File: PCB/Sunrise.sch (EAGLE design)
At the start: 66 parts, among them IC1 STNS01, IC2 MT2492, J2 B2B-PH-K-S, J3 POWER_JACK, M1 E73-2G4M04S, Q1 IRLHM630, Q2 IRLHM630, Q3 IRLHM630

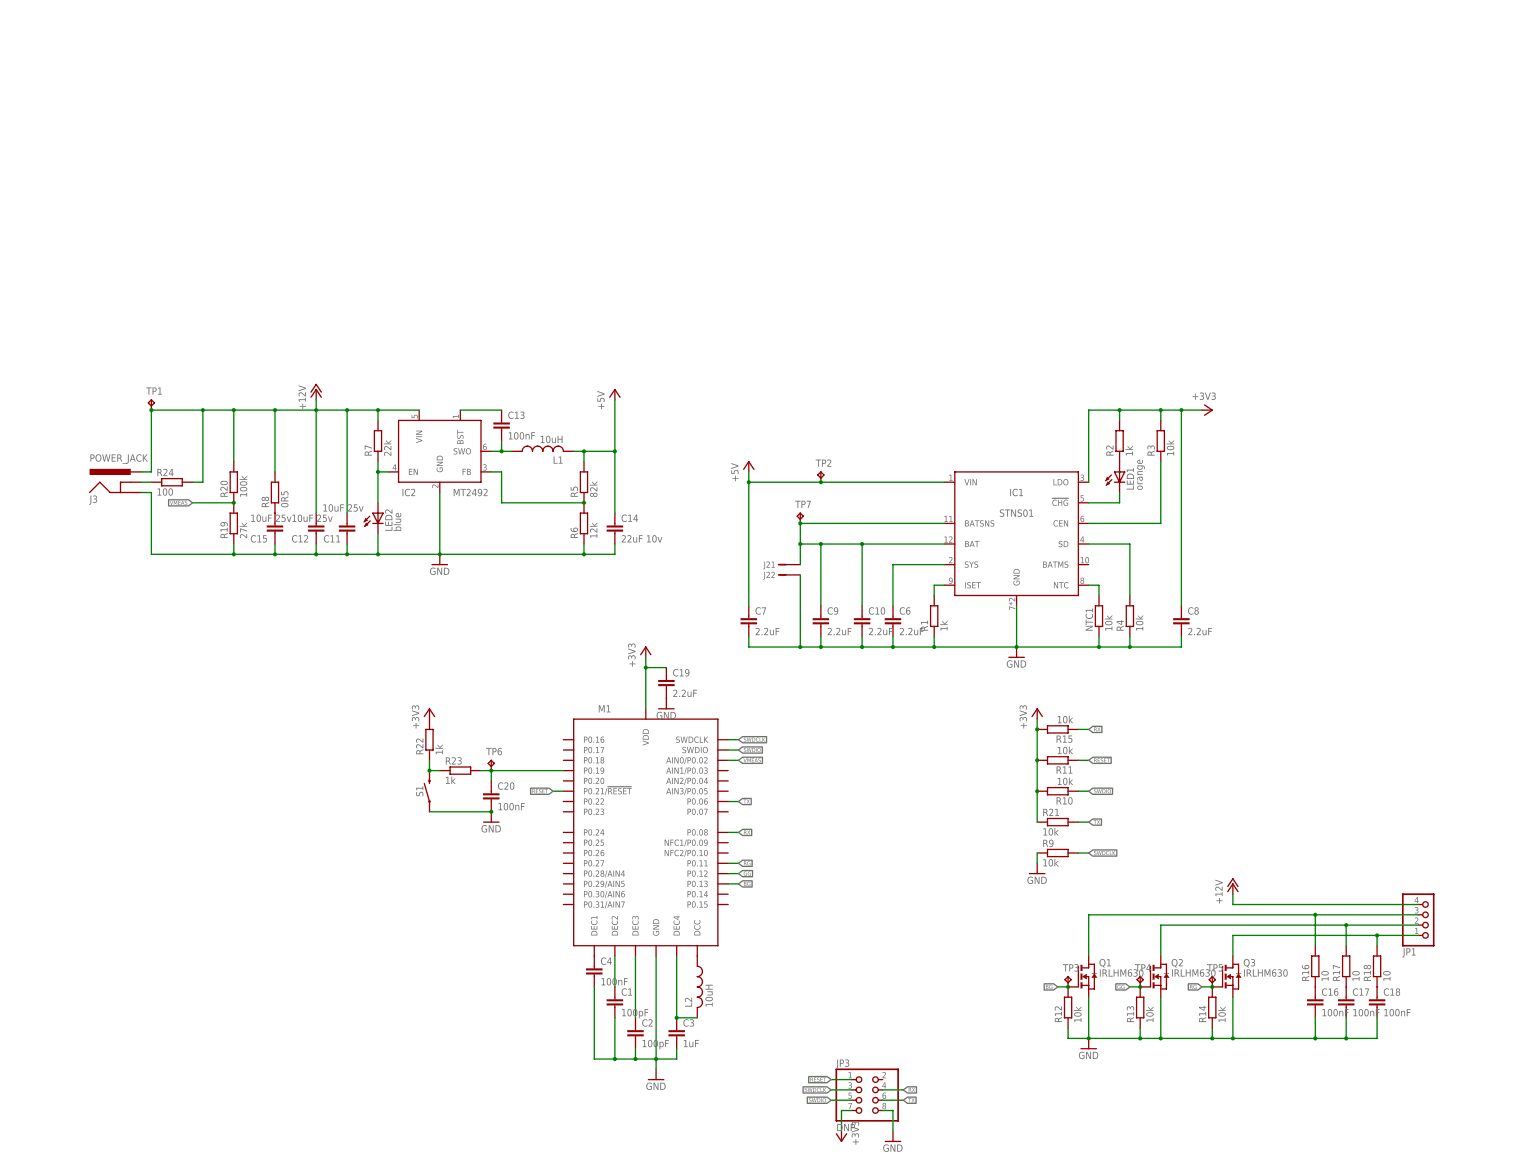
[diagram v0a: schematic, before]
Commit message: PCB: Clean schematic, move values on board around a bit, no actual connectivity or component changes
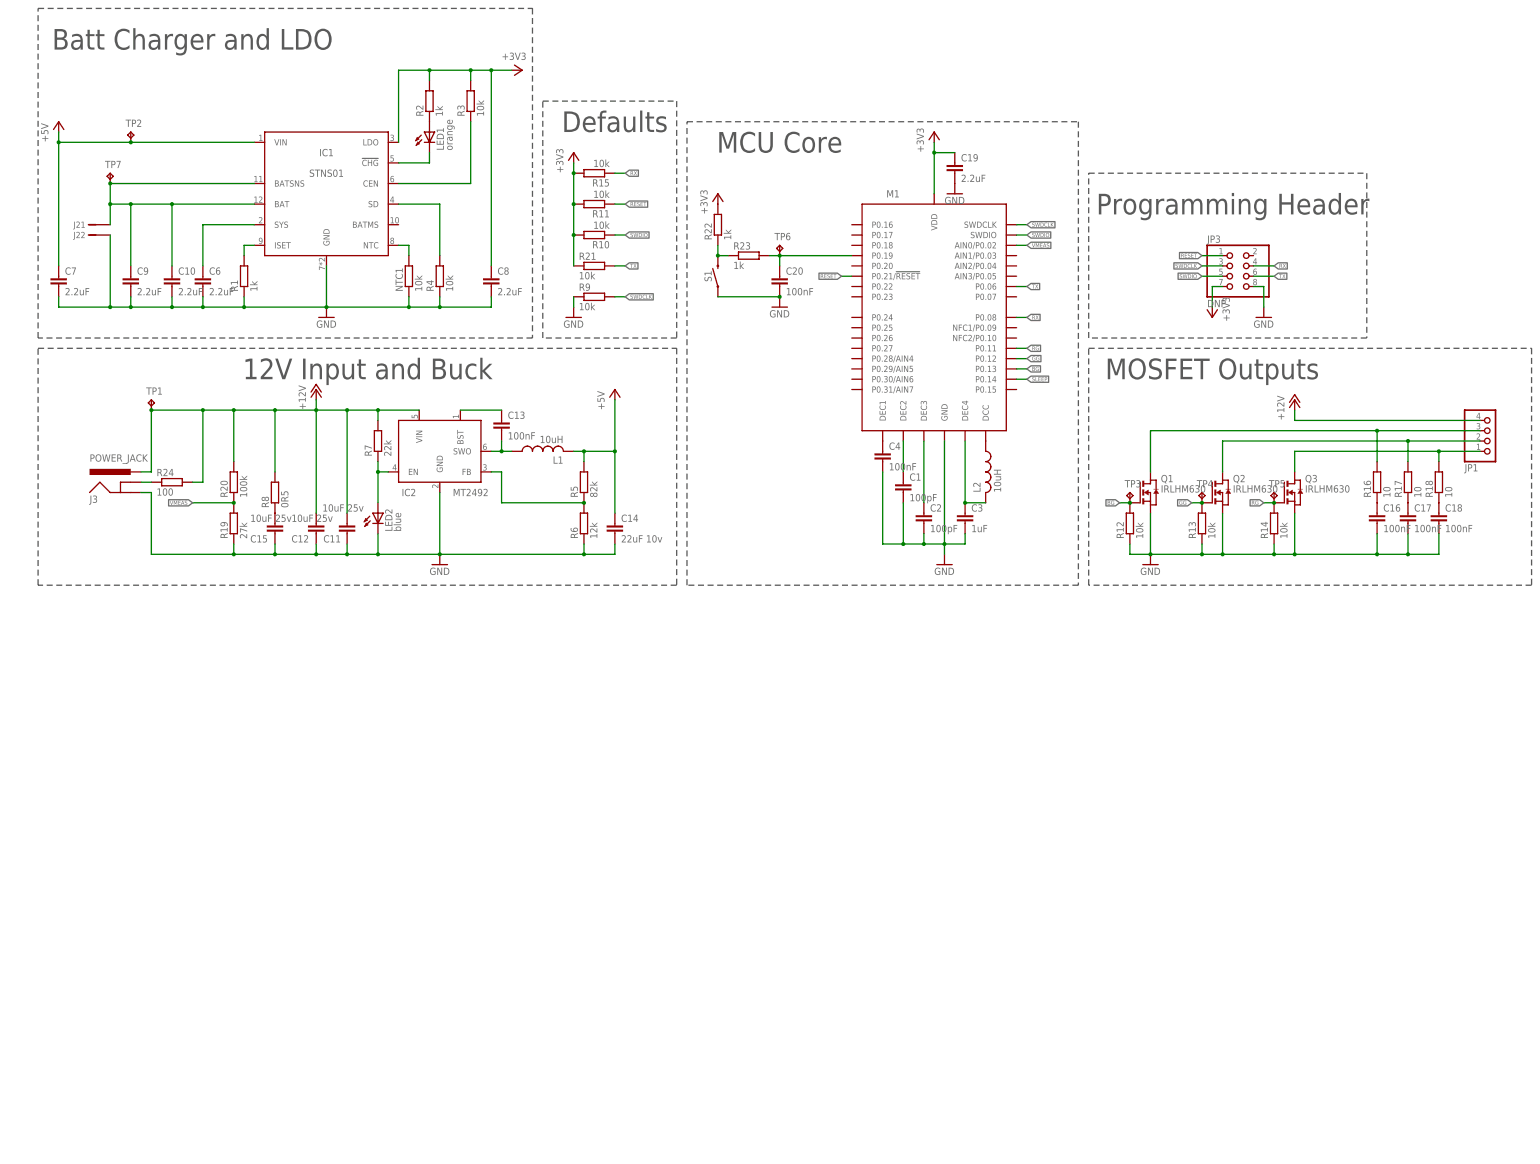
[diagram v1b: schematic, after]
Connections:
- new net SLEEP: M1.P0.14
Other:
- note added: "12V Input and Buck"
- note added: "Batt Charger and LDO"
- note added: "Defaults"
- note added: "MCU Core"
- note added: "MOSFET Outputs"
- note added: "Programming Header"
- moved on the sheet: C1, C10, C16, C17, C18, C19, C2, C20, C3, C4, C6, C7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

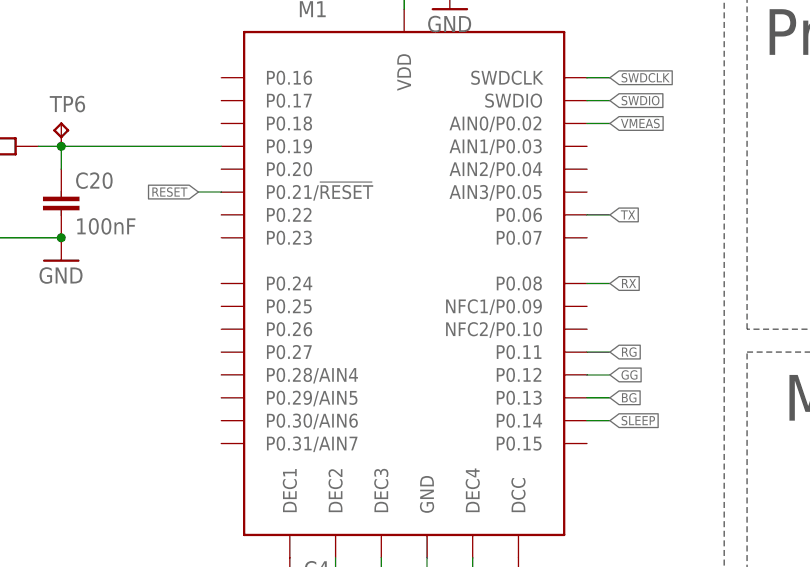
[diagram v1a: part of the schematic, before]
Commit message: PCB: Minor update to NRF52 module; specify a package variant and expand its description
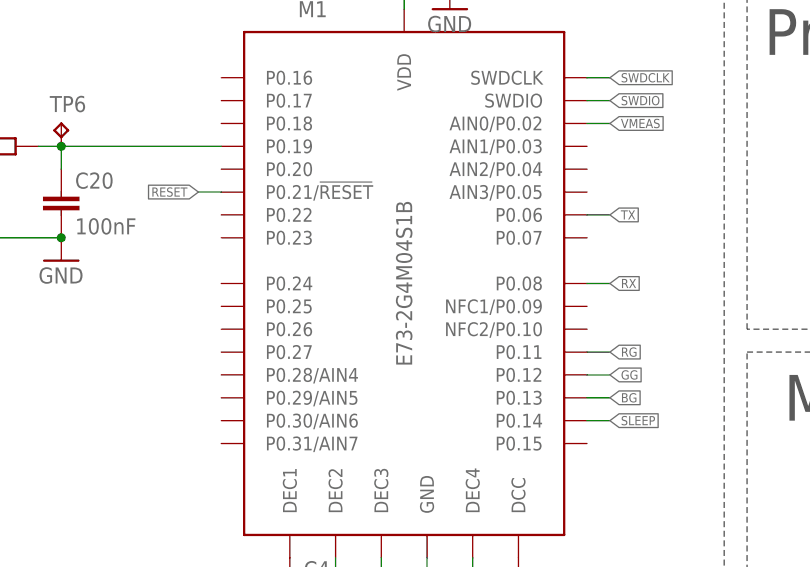
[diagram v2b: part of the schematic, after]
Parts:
- M1: value E73-2G4M04S -> E73-2G4M04S1B; device E73-2G4M04S:E73-2G4M04S -> E73-2G4M04S:E73-2G4M04S1B
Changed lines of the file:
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@@
 </classes>
 <parts>
-<part name="M1" library="E73-2G4M04S" deviceset="E73-2G4M04S" device=""/>
+<part name="M1" library="E73-2G4M04S" deviceset="E73-2G4M04S" device="1B" value="E73-2G4M04S1B"/>
 <part name="GND1" library="supply1" deviceset="GND" device=""/>
 <part name="C1" library="rcl" deviceset="C-EU" device="C0402K" value="100pF"/>

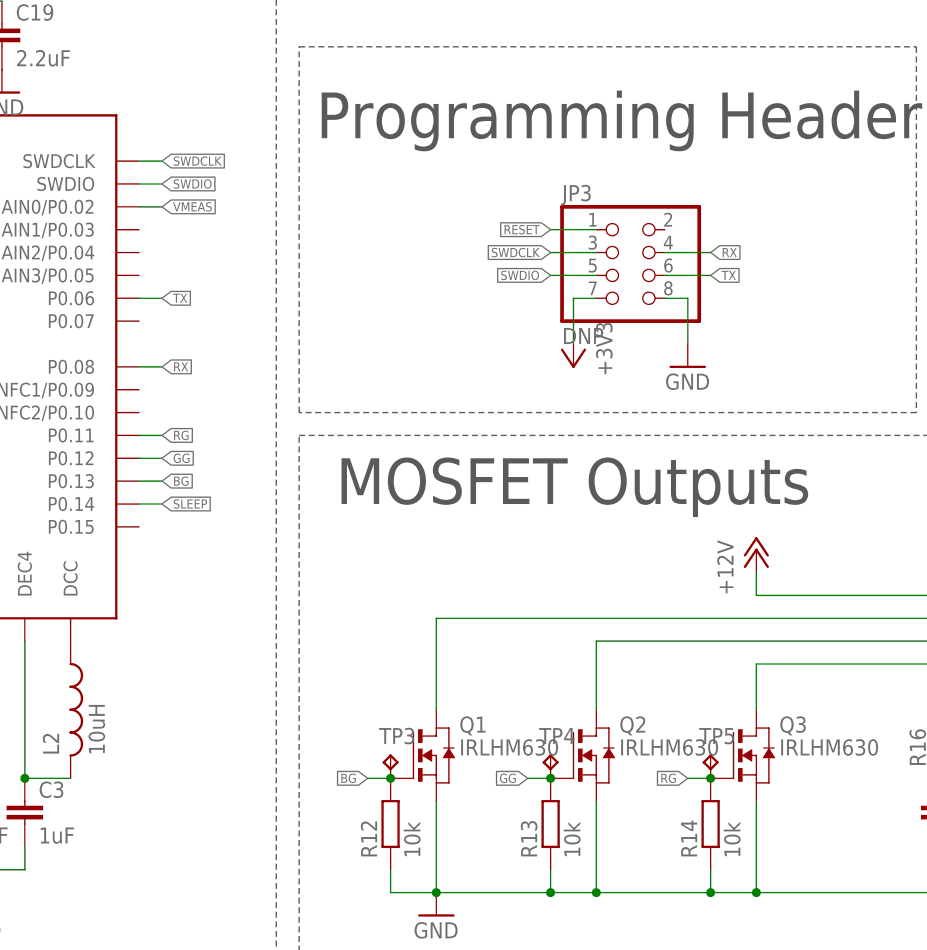
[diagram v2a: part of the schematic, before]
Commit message: Relabel red/green/blue channels to match common RGB strips
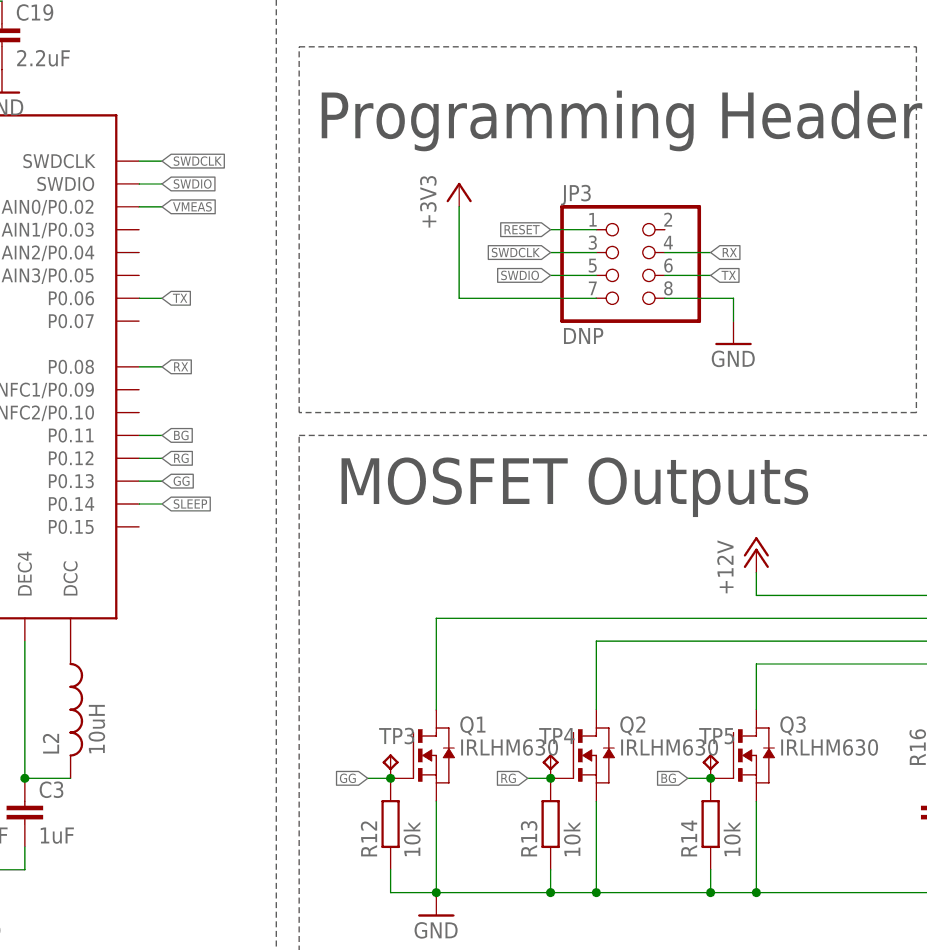
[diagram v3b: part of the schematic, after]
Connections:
- net BG: now also M1.P0.11, Q3.G, R14.2, TP5.TP; no longer M1.P0.13, Q1.G, R12.2, TP3.TP
- net GG: now also M1.P0.13, Q1.G, R12.2, TP3.TP; no longer M1.P0.12, Q2.G, R13.2, TP4.TP
- net RG: now also M1.P0.12, Q2.G, R13.2, TP4.TP; no longer M1.P0.11, Q3.G, R14.2, TP5.TP
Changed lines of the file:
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@@
 <attribute name="NAME" x="64.516" y="185.42" size="1.778" layer="95" font="vector" rot="R90" align="bottom-center"/>
 </instance>
-<instance part="GND9" gate="1" x="200.66" y="175.26"/>
-<instance part="+3V6" gate="G$1" x="187.96" y="175.26" rot="R180"/>
+<instance part="GND9" gate="1" x="205.74" y="177.8"/>
+<instance part="+3V6" gate="G$1" x="175.26" y="195.58"/>
 <instance part="R24" gate="G$1" x="-68.58" y="134.62"/>
 <instance part="L2" gate="G$1" x="132.08" y="137.16"/>
@@
 </segment>
 <segment>
-<wire x1="198.12" y1="182.88" x2="200.66" y2="182.88" width="0.1524" layer="91"/>
+<wire x1="198.12" y1="182.88" x2="205.74" y2="182.88" width="0.1524" layer="91"/>
 <pinref part="GND9" gate="1" pin="GND"/>
-<wire x1="200.66" y1="182.88" x2="200.66" y2="177.8" width="0.1524" layer="91"/>
+<wire x1="205.74" y1="182.88" x2="205.74" y2="180.34" width="0.1524" layer="91"/>
 <pinref part="JP3" gate="A" pin="8"/>
 </segment>
@@
 </segment>
 <segment>
-<wire x1="190.5" y1="182.88" x2="187.96" y2="182.88" width="0.1524" layer="91"/>
+<wire x1="190.5" y1="182.88" x2="175.26" y2="182.88" width="0.1524" layer="91"/>
 <pinref part="+3V6" gate="G$1" pin="+3V3"/>
-<wire x1="187.96" y1="182.88" x2="187.96" y2="177.8" width="0.1524" layer="91"/>
+<wire x1="175.26" y1="182.88" x2="175.26" y2="193.04" width="0.1524" layer="91"/>
 <pinref part="JP3" gate="A" pin="7"/>
 </segment>
@@
 </segment>
 </net>
-<net name="RG" class="0">
+<net name="BG" class="0">
 <segment>
 <pinref part="M1" gate="G$1" pin="P0.11"/>
@@
 </segment>
 </net>
-<net name="GG" class="0">
+<net name="RG" class="0">
 <segment>
 <pinref part="M1" gate="G$1" pin="P0.12"/>
@@
 </segment>
 </net>
-<net name="BG" class="0">
+<net name="GG" class="0">
 <segment>
 <pinref part="M1" gate="G$1" pin="P0.13"/>

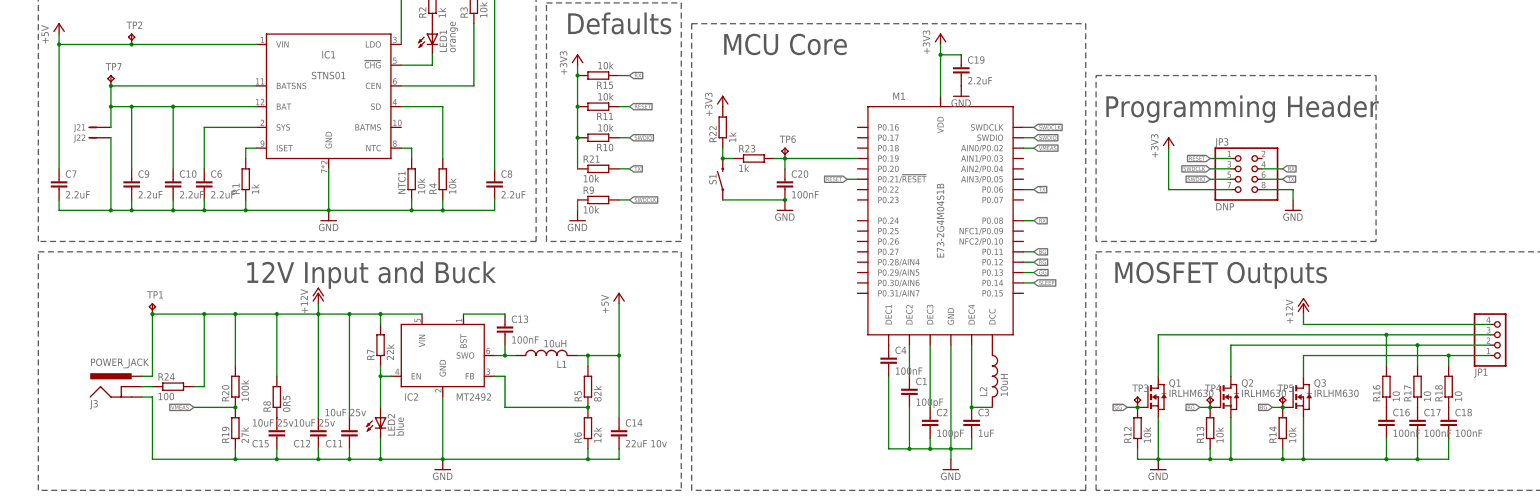
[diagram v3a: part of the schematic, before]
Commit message: Update some footprints, add attributes to several components
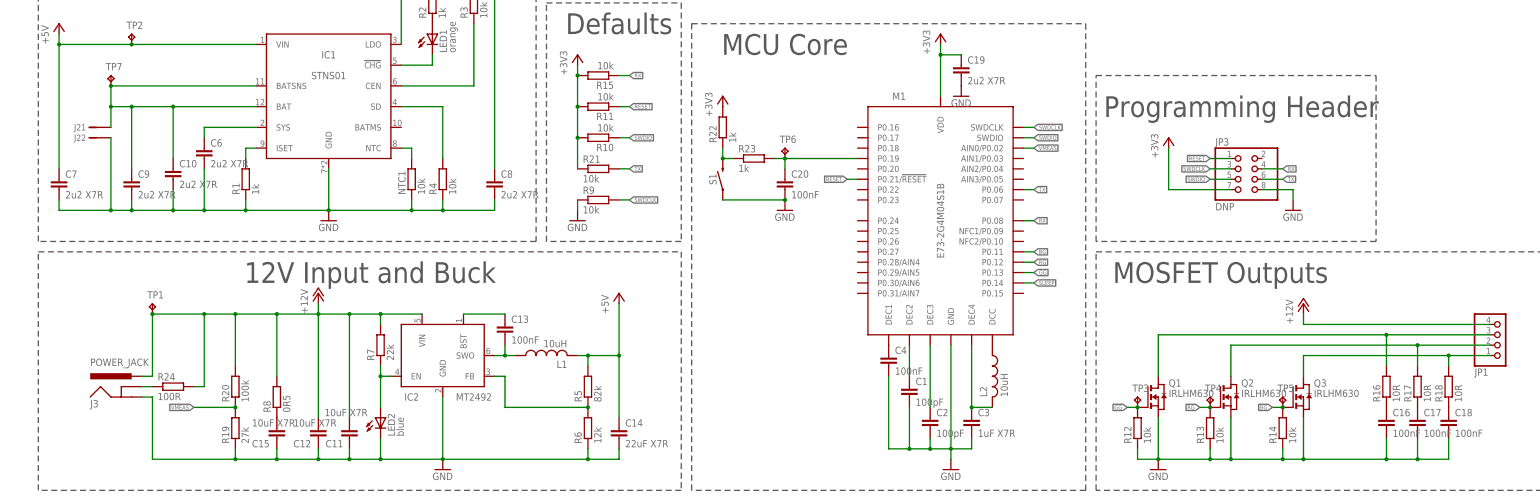
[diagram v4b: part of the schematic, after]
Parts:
- C10, C19, C6, C7, C8, C9: value 2.2uF -> 2u2 X7R
- C11, C12, C15: value 10uF 25v -> 10uF X7R
- C14: value 22uF 10v -> 22uF X7R
- C3: value 1uF -> 1uF X7R
- IC1: MF (none) -> ST; MPN (none) -> STNS01
- IC2: MF (none) -> Monolithic Power; MPN (none) -> MT2492
- J2: MF (none) -> JST; MPN (none) -> B2B-PH-K-S
- L1: MF (none) -> Murata; MPN (none) -> LQH5BPN100MT0; PN LQH5BPN100MT0 -> (none)
- L2: CURRENT (none) -> >50mA
- M1: MF (none) -> Chengdu Ebyte; MPN (none) -> E7302G4M04S1B
- Q1, Q2, Q3: MF (none) -> International Rectifier; MPN (none) -> IRLHM630TRPbF
- R16, R17, R18: value 10 -> 10R
- R24: value 100 -> 100R
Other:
- note added: "0.6v"
- note added: "4.7v"
- note added: "Ichg=200mA"
- moved on the sheet: C10, C6
